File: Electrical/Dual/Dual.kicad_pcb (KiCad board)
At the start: 2 copper layers, 140 x 70 mm, 118 parts, among them J101 01x04, J102 02x04, J103 01x04, J104 01x03, J105 01x03, J106 01x03, J107 01x03, J108 01x03, J109 01x03, J110 01x04, J111 01x04, J112 01x04, J113 01x04, J114 01x03, J115 01x03, J116 01x03, J117 01x03, J201 01x02, J202 01x04, J203 01x03, J204 01x04, J205 01x03, J206 USB_OTG, J207 01x04, J208 01x02, J209 01x04, J210 01x02, J211 01x02, J212 4PostTerm, J213 2PostTerm, J214 2PostTerm, J215 JST_3, J216 2PostTerm, J217 2PostTerm, Q201 FDC6420C, Q202 FDG1024NZ, Q301 FDC6420C, Q401 FDC6420C, U201 TPD4S012, U202 ACS712ELCTR-05B-T, U203 ACS712ELCTR-05B-T, U204 24LC256, U205 LM2576HVS-ADJ, U206 LM2576HVS-ADJ

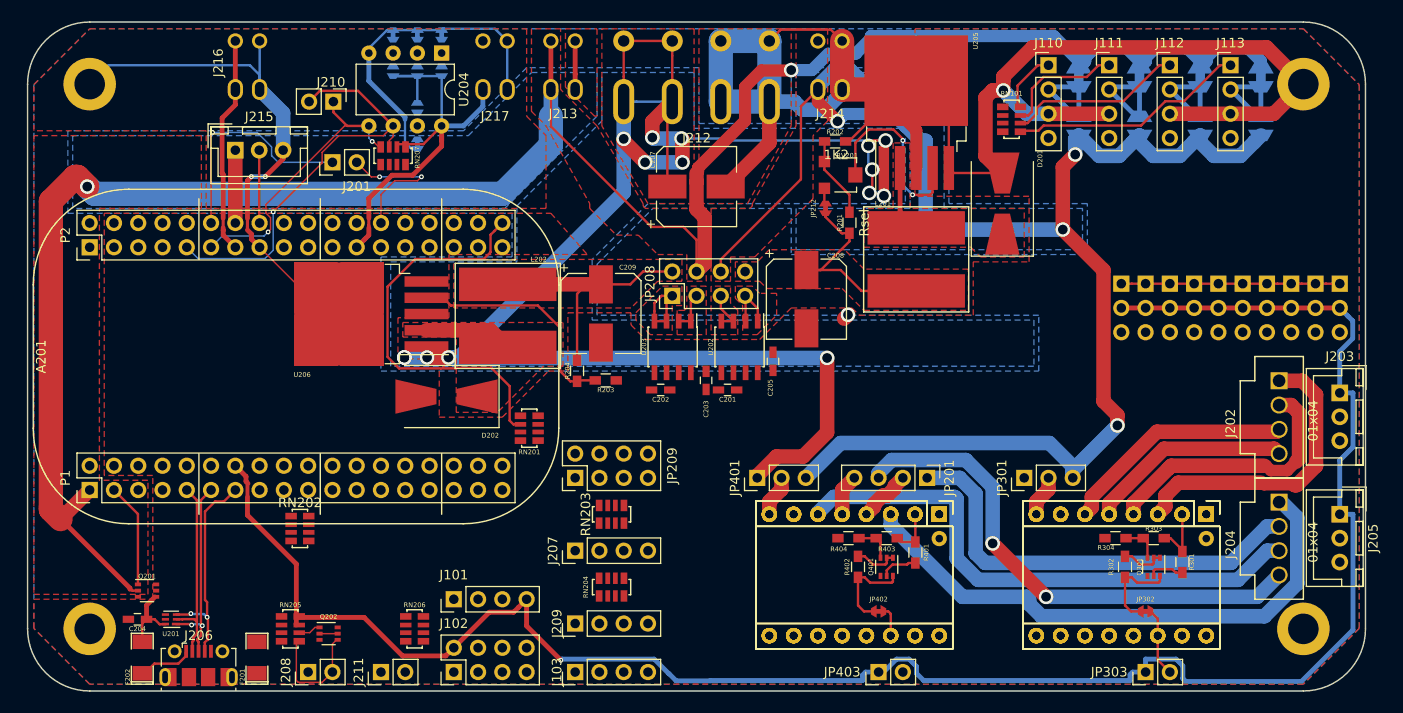
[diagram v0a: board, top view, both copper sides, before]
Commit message: Completed Dual Stepper Layout. TODO: Via stitching.
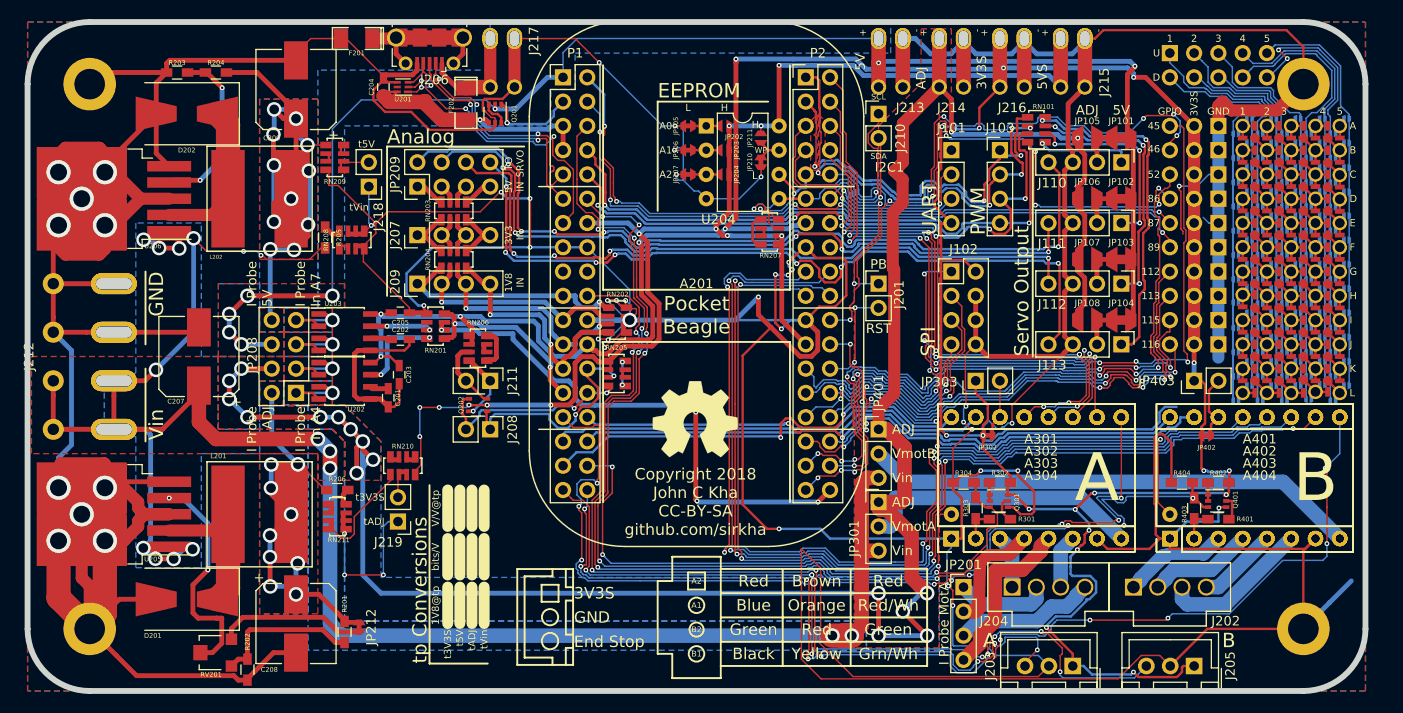
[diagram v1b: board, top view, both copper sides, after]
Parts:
- added J118: 02x05, Pin_Headers:Pin_Header_Straight_2x05_Pitch2.54mm, B.Cu at (149.5, 68.2)
- added J218: 01x02, Pin_Headers:Pin_Header_Straight_1x02_Pitch2.54mm, F.Cu at (65.7, 82.2)
- added J219: 01x02, Pin_Headers:Pin_Header_Straight_1x02_Pitch2.54mm, F.Cu at (68.8, 117.3)
- added R205: 12K, Resistors_SMD:R_0603_HandSoldering, F.Cu at (61.1, 87.6)
- added R206: 12K, Resistors_SMD:R_0603_HandSoldering, F.Cu at (62.4, 114.0)
- added REF***: OSHW-Symbol_8.9x8mm_SilkScreen, Symbols:OSHW-Symbol_8.9x8mm_SilkScreen, F.Cu at (99.8, 106.6)
- added RN208: 1K2, footprints:R_Array_1206x04, F.Cu at (63.9, 87.8)
- added RN209: 1K2, footprints:R_Array_1206x04, F.Cu at (62.2, 79.2)
- added RN210: 1K2, footprints:R_Array_1206x04, F.Cu at (69.3, 111.4)
- added RN211: 1K2, footprints:R_Array_1206x04, F.Cu at (62.4, 116.8)
- added x101: RoutaCell, footprints:RoutaCellTop, F.Cu at (157.2, 75.9)
- added x102: RoutaCell, footprints:RoutaCellLeft, F.Cu at (157.2, 78.4)
- added x103: RoutaCell, footprints:RoutaCellLeft, F.Cu at (157.2, 81.0)
- added x104: RoutaCell, footprints:RoutaCellLeft, F.Cu at (157.2, 83.5)
- added x105: RoutaCell, footprints:RoutaCellLeft, F.Cu at (157.2, 86.0)
- added x106: RoutaCell, footprints:RoutaCellLeft, F.Cu at (157.2, 88.6)
- added x107: RoutaCell, footprints:RoutaCellLeft, F.Cu at (157.2, 91.1)
- added x108: RoutaCell, footprints:RoutaCellLeft, F.Cu at (157.2, 93.5)
- added x109: RoutaCell, footprints:RoutaCellLeft, F.Cu at (157.2, 96.2)
- added x110: RoutaCell, footprints:RoutaCellLeft, F.Cu at (157.2, 98.7)
- added x111: RoutaCell, footprints:RoutaCellLeft, F.Cu at (157.2, 101.3)
- added x112: RoutaCell, footprints:RoutaCellBottomLeft, F.Cu at (157.2, 103.8)
- added x113: RoutaCell, footprints:RoutaCellTop, F.Cu at (159.7, 75.9)
- added x114: RoutaCell, footprints:RoutaCell, F.Cu at (159.7, 78.4)
- added x115: RoutaCell, footprints:RoutaCell, F.Cu at (159.7, 81.0)
- added x116: RoutaCell, footprints:RoutaCell, F.Cu at (159.7, 83.5)
- added x117: RoutaCell, footprints:RoutaCell, F.Cu at (159.7, 86.0)
- added x118: RoutaCell, footprints:RoutaCell, F.Cu at (159.7, 88.6)
- added x119: RoutaCell, footprints:RoutaCell, F.Cu at (159.7, 91.1)
- added x120: RoutaCell, footprints:RoutaCell, F.Cu at (159.7, 93.7)
- added x121: RoutaCell, footprints:RoutaCell, F.Cu at (159.7, 96.2)
- added x122: RoutaCell, footprints:RoutaCell, F.Cu at (159.7, 98.7)
- added x123: RoutaCell, footprints:RoutaCell, F.Cu at (159.7, 101.3)
- added x124: RoutaCell, footprints:RoutaCellBottom, F.Cu at (159.7, 103.8)
- added x125: RoutaCell, footprints:RoutaCellTop, F.Cu at (162.2, 75.9)
- added x126: RoutaCell, footprints:RoutaCell, F.Cu at (162.2, 78.4)
- added x127: RoutaCell, footprints:RoutaCell, F.Cu at (162.2, 81.0)
- added x128: RoutaCell, footprints:RoutaCell, F.Cu at (162.2, 83.5)
- added x129: RoutaCell, footprints:RoutaCell, F.Cu at (162.2, 86.0)
- added x130: RoutaCell, footprints:RoutaCell, F.Cu at (162.2, 88.6)
- added x131: RoutaCell, footprints:RoutaCell, F.Cu at (162.2, 91.1)
- added x132: RoutaCell, footprints:RoutaCell, F.Cu at (162.2, 93.7)
- added x133: RoutaCell, footprints:RoutaCell, F.Cu at (162.2, 96.2)
- added x134: RoutaCell, footprints:RoutaCell, F.Cu at (162.2, 98.7)
- added x135: RoutaCell, footprints:RoutaCell, F.Cu at (162.2, 101.3)
- added x136: RoutaCell, footprints:RoutaCellBottom, F.Cu at (162.2, 103.8)
- added x137: RoutaCell, footprints:RoutaCellTop, F.Cu at (164.8, 75.9)
- added x138: RoutaCell, footprints:RoutaCell, F.Cu at (164.8, 78.4)
- added x139: RoutaCell, footprints:RoutaCell, F.Cu at (164.8, 81.0)
- added x140: RoutaCell, footprints:RoutaCell, F.Cu at (164.8, 83.5)
- added x141: RoutaCell, footprints:RoutaCell, F.Cu at (164.8, 86.0)
- added x142: RoutaCell, footprints:RoutaCell, F.Cu at (164.8, 88.6)
- added x143: RoutaCell, footprints:RoutaCell, F.Cu at (164.8, 91.1)
- added x144: RoutaCell, footprints:RoutaCell, F.Cu at (164.8, 93.7)
- added x145: RoutaCell, footprints:RoutaCell, F.Cu at (164.8, 96.2)
- added x146: RoutaCell, footprints:RoutaCell, F.Cu at (164.8, 98.7)
- added x147: RoutaCell, footprints:RoutaCell, F.Cu at (164.8, 101.3)
- added x148: RoutaCell, footprints:RoutaCellBottom, F.Cu at (164.8, 103.7)
- added x149: RoutaCell, footprints:RoutaCellTopRight, F.Cu at (167.3, 75.9)
- added x150: RoutaCell, footprints:RoutaCellRight, F.Cu at (167.3, 78.4)
- added x151: RoutaCell, footprints:RoutaCellRight, F.Cu at (167.3, 81.0)
- added x152: RoutaCell, footprints:RoutaCellRight, F.Cu at (167.3, 83.5)
- added x153: RoutaCell, footprints:RoutaCellRight, F.Cu at (167.3, 86.0)
- added x154: RoutaCell, footprints:RoutaCellRight, F.Cu at (167.3, 88.6)
- added x155: RoutaCell, footprints:RoutaCellRight, F.Cu at (167.3, 91.1)
- added x156: RoutaCell, footprints:RoutaCellRight, F.Cu at (167.3, 93.7)
- added x157: RoutaCell, footprints:RoutaCellRight, F.Cu at (167.3, 96.2)
- added x158: RoutaCell, footprints:RoutaCellRight, F.Cu at (167.3, 98.7)
- added x159: RoutaCell, footprints:RoutaCellRight, F.Cu at (167.3, 101.3)
- added x160: RoutaCell, footprints:RoutaCellBottomRight, F.Cu at (167.3, 103.8)
- J206: footprint Connectors_USB:USB_Micro-B_Molex-105017-0001 -> footprints:USB_Micro-B_Molex-105017-0001_CircularHoles
- J213, J214, J216, J217, JP101, JP102, JP103, JP104, JP105, JP106, JP107, JP108, JP202, JP203, JP204, JP205, JP206, JP207, JP210, JP211: moved to F.Cu
- J215: value JST_3 -> 2PostTerm; footprint Connectors_JST:JST_XH_B03B-XH-A_03x2.50mm_Straight -> footprints:TerminalBlock_Custom_1x02.54mm
- moved D201 94.9 mm to (46.7, 125.4), turned to 180 degrees
- moved U205 93.9 mm to (39.0, 116.5), turned to 180 degrees
- moved J215 88.1 mm to (139.4, 69.3)
- moved R202 82.7 mm to (53.0, 132.8), turned to 90 degrees
- moved RV201 82.2 mm to (49.7, 131.0), turned to 90 degrees
- moved J216 80.0 mm to (133.0, 69.3)
- moved L201 73.7 mm to (54.3, 116.5), turned to 0 degrees
- moved J206 70.5 mm to (72.1, 67.0), turned to 180 degrees
- moved J103 70.4 mm to (131.8, 78.4), turned to 0 degrees
- moved J101 70.1 mm to (126.7, 78.4), turned to 0 degrees
- moved J212 69.9 mm to (36.5, 100.0), turned to 270 degrees
- moved R201 68.0 mm to (63.2, 128.8), turned to 270 degrees
- moved F202 67.1 mm to (75.9, 73.6), turned to 270 degrees
- moved J102 66.8 mm to (126.7, 91.1), turned to 0 degrees
- moved A201 65.7 mm to (86.0, 70.8), turned to 0 degrees
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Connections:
- A201 pad 2.10: /Common/gpio1_20 -> /gpio1_20
- A201 pad 2.14: +BATT -> Net-(A201-Pad2.14)
- A201 pad 2.16: /Common/batt_temp -> Net-(A201-Pad2.16)
- A201 pad 2.24: /gpio1_12 -> /Common/gpio1_12
- A301 pad 10: /Common/gpio2_0 -> /Common/gpio1_27
- A301 pad 11: /Common/gpio0_27 -> /Common/gpio1_26
- A301 pad 12: /Common/gpio1_15 -> /Common/gpio1_25
- A301 pad 13: /Common/gpio2_1 -> /Common/gpio1_28
- A301 pad 14: /Common/StepperB/SLP -> /Common/StepperA/SLP
- A301 pad 15: /Common/pr1_pru1_pru_r30_15 -> /Common/pr1_pru0_pru_r30_04
- A301 pad 16: /Common/pr1_pru1_pru_r30_14 -> /Common/pr1_pru0_pru_r30_01
- A301 pad 2: /Common/StepperB/fault_supply -> /Common/StepperA/fault_supply
- A301 pad 3: /Common/StepperB/A2 -> /Common/StepperA/A2
- A301 pad 4: /Common/StepperB/A1 -> /Common/StepperA/A1
- A301 pad 5: /Common/StepperB/B1 -> /Common/StepperA/B1
- A301 pad 6: /Common/StepperB/B2 -> /Common/StepperA/B2
- A301 pad 8: /Common/StepperB/Vmot -> /Common/StepperA/Vmot
- A301 pad 9: /Common/pr1_pru0_pru_r30_00 -> /Common/pr1_pru0_pru_r30_07
- A302 pad 10: /Common/gpio2_0 -> /Common/gpio1_27
- A302 pad 11: /Common/gpio0_27 -> /Common/gpio1_26
- A302 pad 12: /Common/gpio1_15 -> /Common/gpio1_25
- A302 pad 13: /Common/gpio2_1 -> /Common/gpio1_28
- A302 pad 14: /Common/StepperB/SLP -> /Common/StepperA/SLP
- A302 pad 15: /Common/pr1_pru1_pru_r30_15 -> /Common/pr1_pru0_pru_r30_04
- A302 pad 16: /Common/pr1_pru1_pru_r30_14 -> /Common/pr1_pru0_pru_r30_01
- A302 pad 2: /Common/StepperB/fault_supply -> /Common/StepperA/fault_supply
- A302 pad 3: /Common/StepperB/A2 -> /Common/StepperA/A2
- A302 pad 4: /Common/StepperB/A1 -> /Common/StepperA/A1
- A302 pad 5: /Common/StepperB/B1 -> /Common/StepperA/B1
- A302 pad 6: /Common/StepperB/B2 -> /Common/StepperA/B2
- A302 pad 8: /Common/StepperB/Vmot -> /Common/StepperA/Vmot
- A302 pad 9: /Common/pr1_pru0_pru_r30_00 -> /Common/pr1_pru0_pru_r30_07
- A303 pad 10: /Common/gpio2_0 -> /Common/gpio1_27
- A303 pad 11: /Common/gpio0_27 -> /Common/gpio1_26
- A303 pad 12: /Common/gpio1_15 -> /Common/gpio1_25
- A303 pad 13: /Common/gpio2_1 -> /Common/gpio1_28
- A303 pad 14: /Common/StepperB/SLP -> /Common/StepperA/SLP
- A303 pad 15: /Common/pr1_pru1_pru_r30_15 -> /Common/pr1_pru0_pru_r30_04
- A303 pad 16: /Common/pr1_pru1_pru_r30_14 -> /Common/pr1_pru0_pru_r30_01
- A303 pad 2: /Common/StepperB/fault_supply -> /Common/StepperA/fault_supply
- A303 pad 3: /Common/StepperB/A2 -> /Common/StepperA/A2
- A303 pad 4: /Common/StepperB/A1 -> /Common/StepperA/A1
- A303 pad 5: /Common/StepperB/B1 -> /Common/StepperA/B1
- A303 pad 6: /Common/StepperB/B2 -> /Common/StepperA/B2
- A303 pad 8: /Common/StepperB/Vmot -> /Common/StepperA/Vmot
- A303 pad 9: /Common/pr1_pru0_pru_r30_00 -> /Common/pr1_pru0_pru_r30_07
- A304 pad 10: /Common/gpio2_0 -> /Common/gpio1_27
- A304 pad 11: /Common/gpio0_27 -> /Common/gpio1_26
- A304 pad 12: /Common/gpio1_15 -> /Common/gpio1_25
- A304 pad 13: /Common/gpio2_1 -> /Common/gpio1_28
- A304 pad 14: /Common/StepperB/SLP -> /Common/StepperA/SLP
- A304 pad 15: /Common/pr1_pru1_pru_r30_15 -> /Common/pr1_pru0_pru_r30_04
- A304 pad 16: /Common/pr1_pru1_pru_r30_14 -> /Common/pr1_pru0_pru_r30_01
- A304 pad 17: /Common/gpio1_28 -> /Common/gpio0_26
- A304 pad 2: /Common/StepperB/fault_supply -> /Common/StepperA/fault_supply
- A304 pad 3: /Common/StepperB/A2 -> /Common/StepperA/A2
- A304 pad 4: /Common/StepperB/A1 -> /Common/StepperA/A1
- A304 pad 5: /Common/StepperB/B1 -> /Common/StepperA/B1
- A304 pad 6: /Common/StepperB/B2 -> /Common/StepperA/B2
- A304 pad 8: /Common/StepperB/Vmot -> /Common/StepperA/Vmot
- A304 pad 9: /Common/pr1_pru0_pru_r30_00 -> /Common/pr1_pru0_pru_r30_07
- A401 pad 10: /Common/gpio1_27 -> /Common/gpio2_0
- A401 pad 11: /Common/gpio1_26 -> /Common/gpio0_27
- A401 pad 12: /Common/gpio1_25 -> /Common/gpio1_15
- A401 pad 13: /Common/gpio1_20 -> /Common/gpio2_1
- A401 pad 14: /Common/StepperA/SLP -> /Common/StepperB/SLP
- A401 pad 15: /Common/pr1_pru0_pru_r30_04 -> /Common/pr1_pru1_pru_r30_15
- A401 pad 16: /Common/pr1_pru0_pru_r30_01 -> /Common/pr1_pru1_pru_r30_14
- A401 pad 2: /Common/StepperA/fault_supply -> /Common/StepperB/fault_supply
- A401 pad 3: /Common/StepperA/A2 -> /Common/StepperB/A2
- A401 pad 4: /Common/StepperA/A1 -> /Common/StepperB/A1
- A401 pad 5: /Common/StepperA/B1 -> /Common/StepperB/B1
- A401 pad 6: /Common/StepperA/B2 -> /Common/StepperB/B2
- A401 pad 8: /Common/StepperA/Vmot -> /Common/StepperB/Vmot
- A401 pad 9: /Common/pr1_pru0_pru_r30_07 -> /Common/pr1_pru0_pru_r30_00
- A402 pad 10: /Common/gpio1_27 -> /Common/gpio2_0
- A402 pad 11: /Common/gpio1_26 -> /Common/gpio0_27
- A402 pad 12: /Common/gpio1_25 -> /Common/gpio1_15
- A402 pad 13: /Common/gpio1_20 -> /Common/gpio2_1
- A402 pad 14: /Common/StepperA/SLP -> /Common/StepperB/SLP
- A402 pad 15: /Common/pr1_pru0_pru_r30_04 -> /Common/pr1_pru1_pru_r30_15
- A402 pad 16: /Common/pr1_pru0_pru_r30_01 -> /Common/pr1_pru1_pru_r30_14
- A402 pad 2: /Common/StepperA/fault_supply -> /Common/StepperB/fault_supply
- A402 pad 3: /Common/StepperA/A2 -> /Common/StepperB/A2
- A402 pad 4: /Common/StepperA/A1 -> /Common/StepperB/A1
- A402 pad 5: /Common/StepperA/B1 -> /Common/StepperB/B1
- A402 pad 6: /Common/StepperA/B2 -> /Common/StepperB/B2
- A402 pad 8: /Common/StepperA/Vmot -> /Common/StepperB/Vmot
- A402 pad 9: /Common/pr1_pru0_pru_r30_07 -> /Common/pr1_pru0_pru_r30_00
- A403 pad 10: /Common/gpio1_27 -> /Common/gpio2_0
- A403 pad 11: /Common/gpio1_26 -> /Common/gpio0_27
- A403 pad 12: /Common/gpio1_25 -> /Common/gpio1_15
- A403 pad 13: /Common/gpio1_20 -> /Common/gpio2_1
- A403 pad 14: /Common/StepperA/SLP -> /Common/StepperB/SLP
- A403 pad 15: /Common/pr1_pru0_pru_r30_04 -> /Common/pr1_pru1_pru_r30_15
- A403 pad 16: /Common/pr1_pru0_pru_r30_01 -> /Common/pr1_pru1_pru_r30_14
- A403 pad 2: /Common/StepperA/fault_supply -> /Common/StepperB/fault_supply
- A403 pad 3: /Common/StepperA/A2 -> /Common/StepperB/A2
- A403 pad 4: /Common/StepperA/A1 -> /Common/StepperB/A1
- A403 pad 5: /Common/StepperA/B1 -> /Common/StepperB/B1
- A403 pad 6: /Common/StepperA/B2 -> /Common/StepperB/B2
- A403 pad 8: /Common/StepperA/Vmot -> /Common/StepperB/Vmot
- A403 pad 9: /Common/pr1_pru0_pru_r30_07 -> /Common/pr1_pru0_pru_r30_00
- A404 pad 10: /Common/gpio1_27 -> /Common/gpio2_0
- A404 pad 11: /Common/gpio1_26 -> /Common/gpio0_27
- A404 pad 12: /Common/gpio1_25 -> /Common/gpio1_15
- A404 pad 13: /Common/gpio1_20 -> /Common/gpio2_1
- A404 pad 14: /Common/StepperA/SLP -> /Common/StepperB/SLP
- A404 pad 15: /Common/pr1_pru0_pru_r30_04 -> /Common/pr1_pru1_pru_r30_15
- A404 pad 16: /Common/pr1_pru0_pru_r30_01 -> /Common/pr1_pru1_pru_r30_14
- A404 pad 17: /Common/gpio0_26 -> /Common/gpio1_12
- A404 pad 2: /Common/StepperA/fault_supply -> /Common/StepperB/fault_supply
- A404 pad 3: /Common/StepperA/A2 -> /Common/StepperB/A2
- A404 pad 4: /Common/StepperA/A1 -> /Common/StepperB/A1
- A404 pad 5: /Common/StepperA/B1 -> /Common/StepperB/B1
- A404 pad 6: /Common/StepperA/B2 -> /Common/StepperB/B2
- A404 pad 8: /Common/StepperA/Vmot -> /Common/StepperB/Vmot
- A404 pad 9: /Common/pr1_pru0_pru_r30_07 -> /Common/pr1_pru0_pru_r30_00
- C204 pad 1: Net-(C204-Pad1) -> /Common/usb1_vbus
- F202 pad 1: Net-(F202-Pad1) -> /Common/usb1_5V
- F202 pad 2: Net-(C204-Pad1) -> /Common/usb1_vbus
- J104 pad 3: /gpio1_12 -> /gpio1_13
- J105 pad 3: /gpio1_13 -> /gpio1_14
- J106 pad 3: /gpio1_14 -> /gpio1_20
- J206 pad 1: Net-(F202-Pad1) -> /Common/usb1_5V
- J208 pad 1: /Common/i2c2_scl -> /Common/i2c2_sda
- J208 pad 2: /Common/i2c2_sda -> /Common/i2c2_scl
- J210 pad 1: /Common/i2c1_sda -> /Common/i2c1_scl
- J210 pad 2: /Common/i2c1_scl -> /Common/i2c1_sda
- J215 pad 1: +BATT -> 5VS
- J215 pad 2: /Common/batt_temp -> GND
- J216 pad 1: 5VS -> 3V3S
- J217 pad 1: 3V3S -> /Common/usb1_5V
- JP208 pad b1: /Common/IP_5V -> /Common/IP_vadj
- JP208 pad b2: +5V -> Vadj
- JP208 pad b3: Vadj -> +5V
- JP208 pad b4: /Common/IP_vadj -> /Common/IP_5V
- JP301 pad 1: Vin -> Vadj
- JP301 pad 2: /Common/StepperB/Vmot -> /Common/StepperA/Vmot
- JP301 pad 3: Vadj -> Vin
- JP302 pad 1: /Common/StepperB/SLP -> /Common/StepperA/SLP
- JP303 pad 2: /Common/StepperB/SLP -> /Common/StepperA/SLP
- JP401 pad 1: Vin -> Vadj
- JP401 pad 2: /Common/StepperA/Vmot -> /Common/StepperB/Vmot
- JP401 pad 3: Vadj -> Vin
- JP402 pad 1: /Common/StepperA/SLP -> /Common/StepperB/SLP
- JP403 pad 2: /Common/StepperA/SLP -> /Common/StepperB/SLP
- Q201 pad 4: Net-(C204-Pad1) -> /Common/usb1_vbus
- Q202 pad 3: Net-(J211-Pad2) -> Net-(J211-Pad1)
- Q202 pad 6: Net-(J211-Pad1) -> Net-(J211-Pad2)
- Q301 pad 3: /Common/gpio0_4 -> /Common/gpio0_5
- Q401 pad 3: /Common/gpio0_5 -> /Common/gpio0_4
- R301 pad 1: /Common/StepperB/fault_supply -> /Common/StepperA/fault_supply
- R303 pad 1: /Common/gpio0_4 -> /Common/gpio0_5
- R303 pad 2: /Common/StepperB/fault_supply -> /Common/StepperA/fault_supply
- R304 pad 1: /Common/gpio0_4 -> /Common/gpio0_5
- R401 pad 1: /Common/StepperA/fault_supply -> /Common/StepperB/fault_supply
- R403 pad 1: /Common/gpio0_5 -> /Common/gpio0_4
- R403 pad 2: /Common/StepperA/fault_supply -> /Common/StepperB/fault_supply
- R404 pad 1: /Common/gpio0_5 -> /Common/gpio0_4
- RN101 pad 1: /ehrpwm0A -> /ehrpwm2B
- RN101 pad 2: /ehrpwm0B -> /ehrpwm1A
- RN101 pad 3: /ehrpwm1A -> /ehrpwm0B
- RN101 pad 4: /ehrpwm2B -> /ehrpwm0A
- RN101 pad 5: Net-(J113-Pad1) -> Net-(J110-Pad1)
- RN101 pad 6: Net-(J112-Pad1) -> Net-(J111-Pad1)
- RN101 pad 7: Net-(J111-Pad1) -> Net-(J112-Pad1)
- RN101 pad 8: Net-(J110-Pad1) -> Net-(J113-Pad1)
- RN205 pad 1: Net-(RN205-Pad1) -> 3V3S
- RN205 pad 2: Net-(RN205-Pad2) -> 3V3S
- RN205 pad 3: Net-(RN205-Pad2) -> /Common/i2c2_sda
- RN205 pad 4: Net-(RN205-Pad1) -> /Common/i2c2_scl
- RN205 pad 5: /Common/i2c2_sda -> Net-(RN205-Pad5)
- RN205 pad 6: /Common/i2c2_scl -> Net-(RN205-Pad6)
- RN205 pad 7: 3V3S -> Net-(RN205-Pad6)
- RN205 pad 8: 3V3S -> Net-(RN205-Pad5)
- RN206 pad 3: Net-(J211-Pad1) -> Net-(J211-Pad2)
- RN206 pad 4: Net-(J211-Pad2) -> Net-(J211-Pad1)
- U201 pad 6: Net-(C204-Pad1) -> /Common/usb1_vbus
- U202 pad 1: Net-(JP208-Pada4) -> Net-(JP208-Pada2)
- U202 pad 2: Net-(JP208-Pada4) -> Net-(JP208-Pada2)
- U202 pad 3: Net-(JP208-Pada3) -> Net-(JP208-Pada1)
- U202 pad 4: Net-(JP208-Pada3) -> Net-(JP208-Pada1)
- U203 pad 1: Net-(JP208-Pada2) -> Net-(JP208-Pada4)
- U203 pad 2: Net-(JP208-Pada2) -> Net-(JP208-Pada4)
- U203 pad 3: Net-(JP208-Pada1) -> Net-(JP208-Pada3)
- U203 pad 4: Net-(JP208-Pada1) -> Net-(JP208-Pada3)
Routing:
- net GND: track 282.3 -> 1007.0 mm, vias 3 -> 43
- net /Common/gpio0_4: track 4.04 -> 125.2 mm, vias 0 -> 10
- net /Common/pr1_pru0_pru_r30_00: track 0.00 -> 119.6 mm, vias 0 -> 10
- net /Common/pr1_pru0_pru_r31_16: track 0.00 -> 113.4 mm, vias 0 -> 9
- net /Common/gpio2_0: track 0.00 -> 112.8 mm, vias 0 -> 5
- net /Common/gpio1_15: track 0.00 -> 111.5 mm, vias 0 -> 4
- net 5VS: track 22.7 -> 134.2 mm, vias 0 -> 6
- net /Common/gpio0_27: track 0.00 -> 109.4 mm, vias 0 -> 4
- net /Common/gpio2_1: track 0.00 -> 108.2 mm, vias 0 -> 4
- net /Common/gpio0_5: track 4.04 -> 107.1 mm, vias 0 -> 6
- net /Common/pr1_pru0_pru_r30_07: track 0.00 -> 100.9 mm, vias 0 -> 8
- net /ain_0: track 0.00 -> 88.7 mm, vias 0 -> 5
- net /ain_3: track 0.00 -> 83.0 mm, vias 0 -> 7
- net /gpio1_13: track 0.00 -> 82.0 mm, vias 0 -> 7
- net 3V3S: track 275.8 -> 356.8 mm, vias 1 -> 30
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- added copper zone on B.Cu, net /Common/IP_5V
- added copper zone on B.Cu, net /Common/IP_vadj
- added copper zone on F.Cu, net /ehrpwm1A
- added copper zone on F.Cu, net /ehrpwm2B
- added copper zone on B.Cu, net Net-(JP208-Pada1)
- added copper zone on B.Cu, net Net-(JP208-Pada2)
- added copper zone on B.Cu, net Net-(JP208-Pada3)
- added copper zone on B.Cu, net Net-(JP208-Pada4)
- removed copper zone on F.Cu, net Net-(D201-Pad1)
- removed copper zone on F.Cu, net Net-(D202-Pad1)
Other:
- outline, holes or cut-outs redrawn
- rule trace_min: 0.1524 -> 0.152375
- board text added: "+"
- board text added: "-"
- board text added: "1"
- board text added: "112"
- board text added: "113"
- board text added: "115"
- board text added: "116"
- board text added: "1V8 IN"
- board text added: "1V8@tp"
- board text added: "2"
- board text added: "3"
- board text added: "3V3 IN"
- board text added: "3V3S"
- board text added: "4"
- board text added: "45"
- board text added: "46"
- board text added: "5"
- board text added: "52"
- board text added: "5V"
- board text added: "5V IN"
- board text added: "5VS"
- board text added: "86"
- board text added: "87"
- board text added: "89"
- board text added: "A"
- board text added: "A0"
- board text added: "A1"
- board text added: "A2"
- board text added: "ADJ"
- board text added: "Analog"
- board text added: "B"
- board text added: "B1"
- board text added: "B2"
- board text added: "Black"
- board text added: "Blue"
- board text added: "Brown"
- board text added: "C"
- board text added: "Copyright 2018 John C Kha CC-BY-SA github.com/sirkha"
- board text added: "D"
- board text added: "E"
- board text added: "EEPROM"
- board text added: "End Stop"
- board text added: "F"
- board text added: "G"
- board text added: "GND"
- board text added: "GPIO"
- board text added: "Green"
- board text added: "Grn/Wh"
- board text added: "H"
- board text added: "I"
- board text added: "I Probe 5V"
- board text added: "I Probe ADJ"
- board text added: "I Probe In A4"
- board text added: "I Probe In A7"
- board text added: "I Probe MotA"
- board text added: "I2C1"
- board text added: "J"
- board text added: "K"
- board text added: "L"
- board text added: "Orange"
- board text added: "PB"
- board text added: "PWM"
- board text added: "Pocket Beagle"
- board text added: "Prototyping area inspired by Routaboard. routaboard.com"
- board text added: "RST"
- board text added: "Red"
- board text added: "Red/Wh"
- board text added: "SCL"
- board text added: "SDA"
- board text added: "SPI"
- board text added: "Servo Output"
- board text added: "TO SRVO"
- board text added: "U"
- board text added: "UART"
- board text added: "V/V@tp"
- board text added: "Vin"
- board text added: "VmotA"
- board text added: "VmotB"
- board text added: "WP"
- board text added: "Yellow"
- board text added: "bits/V"
- board text added: "t3V3S"
- board text added: "t5V"
- board text added: "tADJ"
- board text added: "tVin"
- board text added: "tp Conversions"

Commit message: Vias Stitched
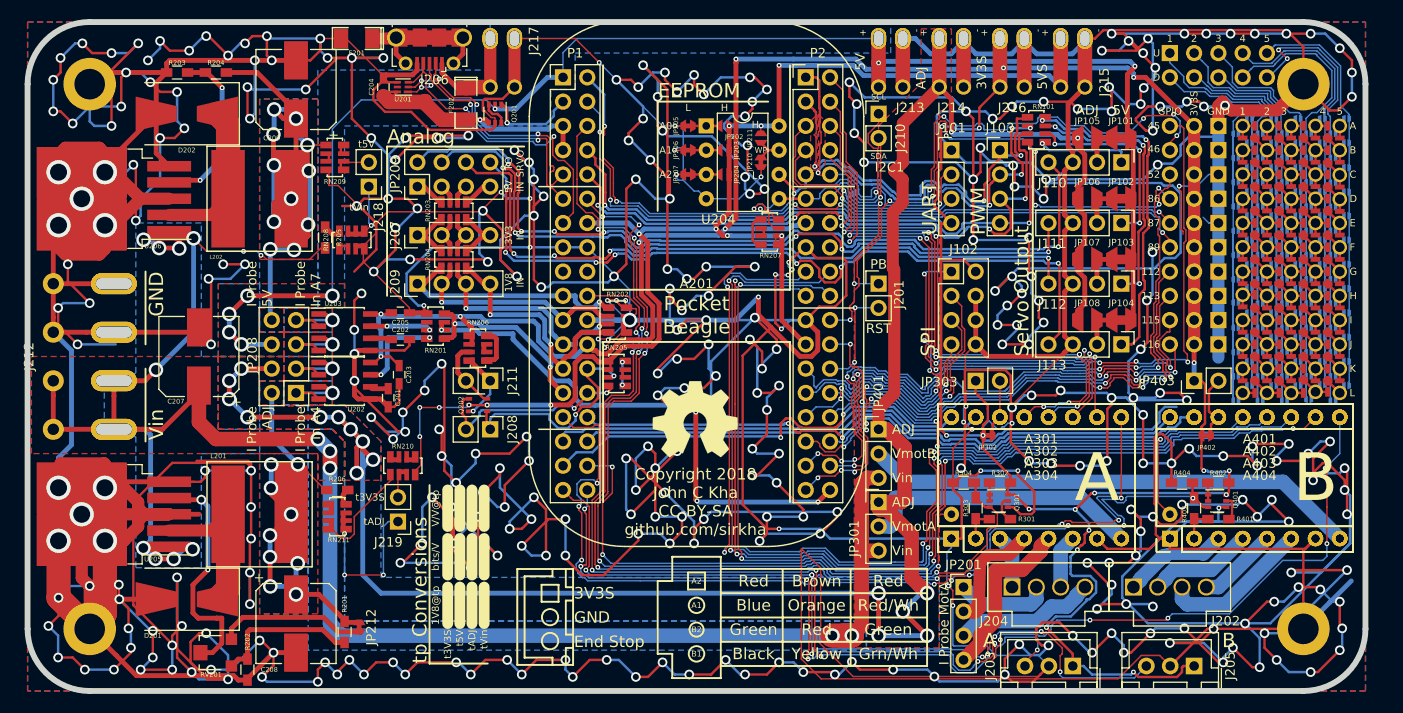
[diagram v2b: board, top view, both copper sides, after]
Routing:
- net GND: track 1007.0 -> 2735.7 mm, vias 43 -> 384
- net Net-(RV201-Pad2): track 23.7 -> 24.7 mm

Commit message: Deleted extranious 3V3S line. Cleaned up tracks as a result.
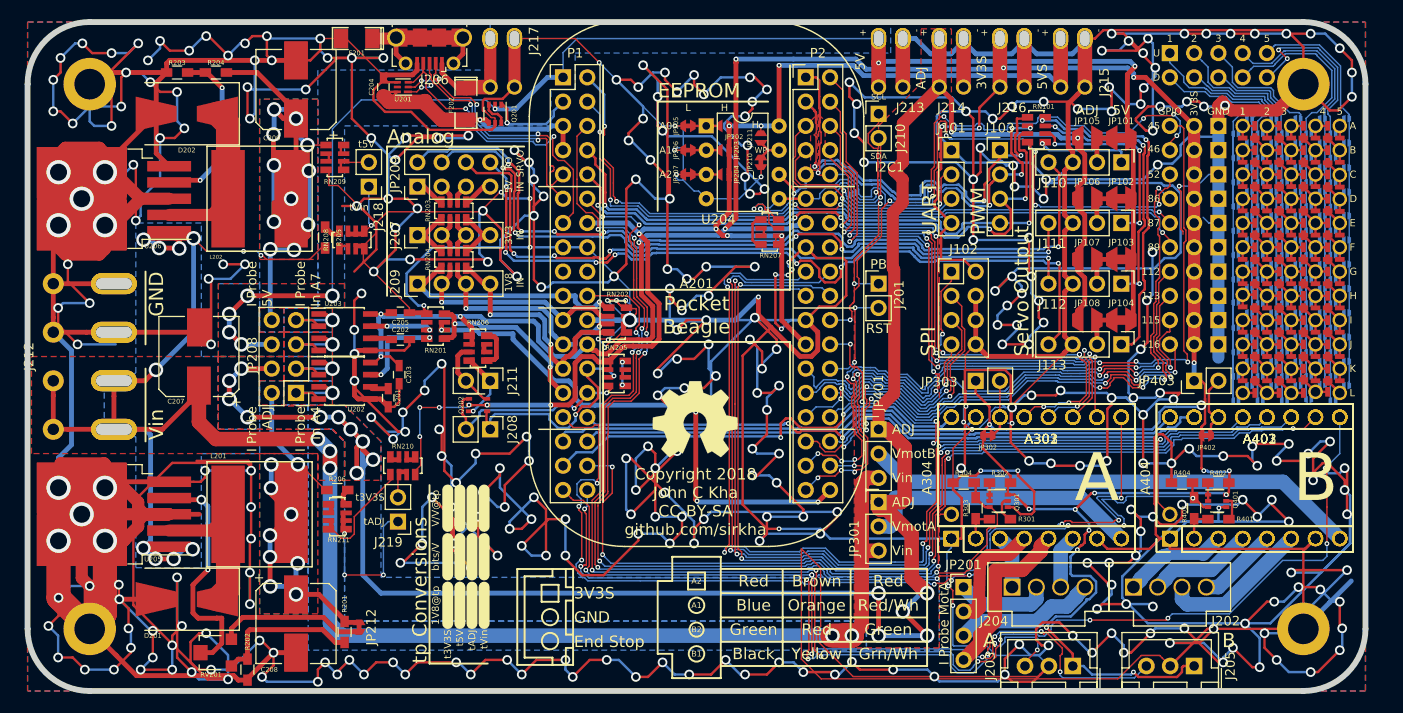
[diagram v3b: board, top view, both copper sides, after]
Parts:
- A301, A302, A303, A401, A402, A403: footprint Modules:Pololu_Breakout-16_15.2x20.3mm -> footprints:Pololu_Breakout-16_15.2x20.3mm
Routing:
- net 3V3S: track 356.8 -> 338.2 mm
- net GND: track 2735.7 -> 2721.5 mm, vias 384 -> 380
- net (no net): track 0.00 -> 13.7 mm, vias 0 -> 4
- net /spi1_d1: track 35.2 -> 32.6 mm, vias 4 -> 3
- net /Common/gpio2_1: track 108.2 -> 107.1 mm
- net /Common/pr1_pru1_pru_r30_14: track 65.1 -> 64.0 mm
- net /Common/pr1_pru1_pru_r30_15: track 69.0 -> 68.0 mm
- net /Common/gpio1_15: track 111.5 -> 110.6 mm
- net /Common/gpio1_27: track 65.0 -> 64.3 mm
- net /Common/gpio0_27: track 109.4 -> 108.8 mm
- net /Common/gpio1_25: track 61.8 -> 61.2 mm
